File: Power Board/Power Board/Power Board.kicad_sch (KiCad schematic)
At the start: 6 parts, among them J1 MINIFIT-2-VERT, J2 NMJ6HFD2, J3 NMJ6HFD2, J4 MEGAFIT-2-VERT, J5 MINIFIT-2-VERT

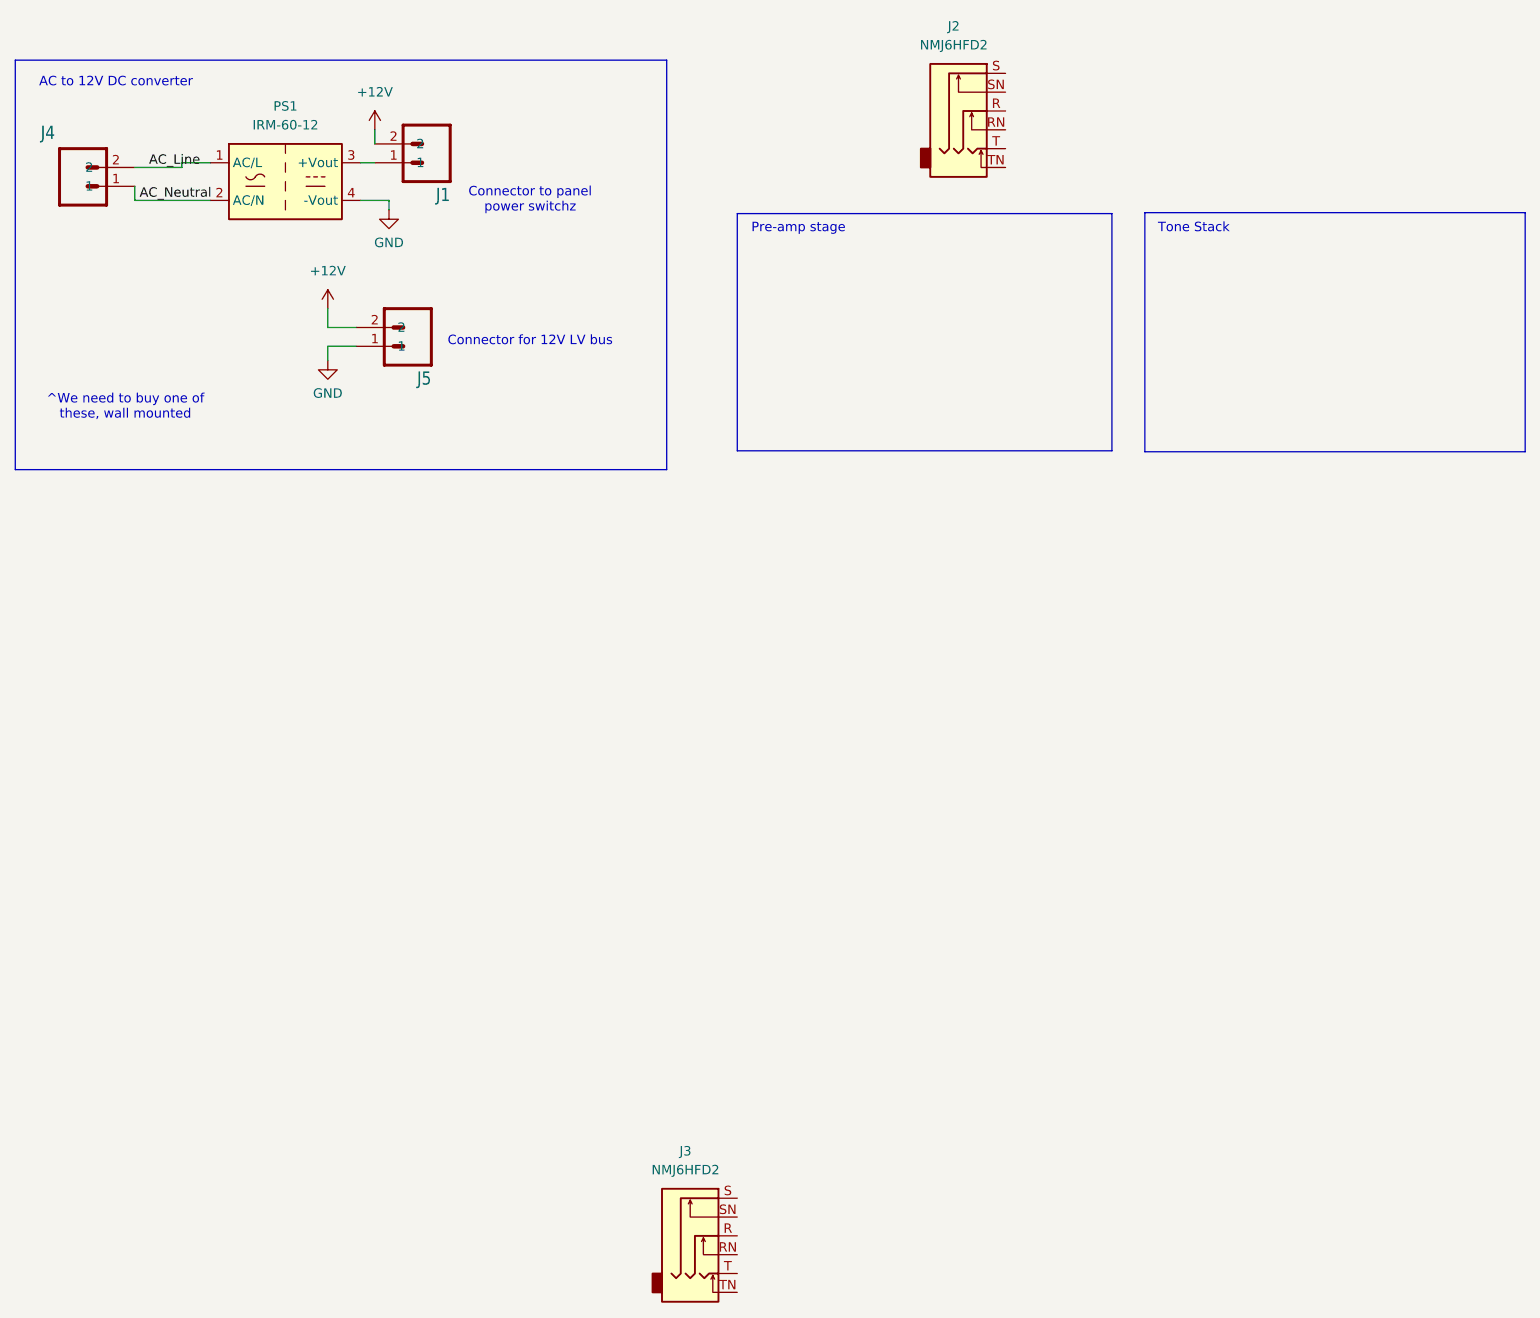
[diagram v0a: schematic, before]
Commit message: Finished schematic and layout of power board
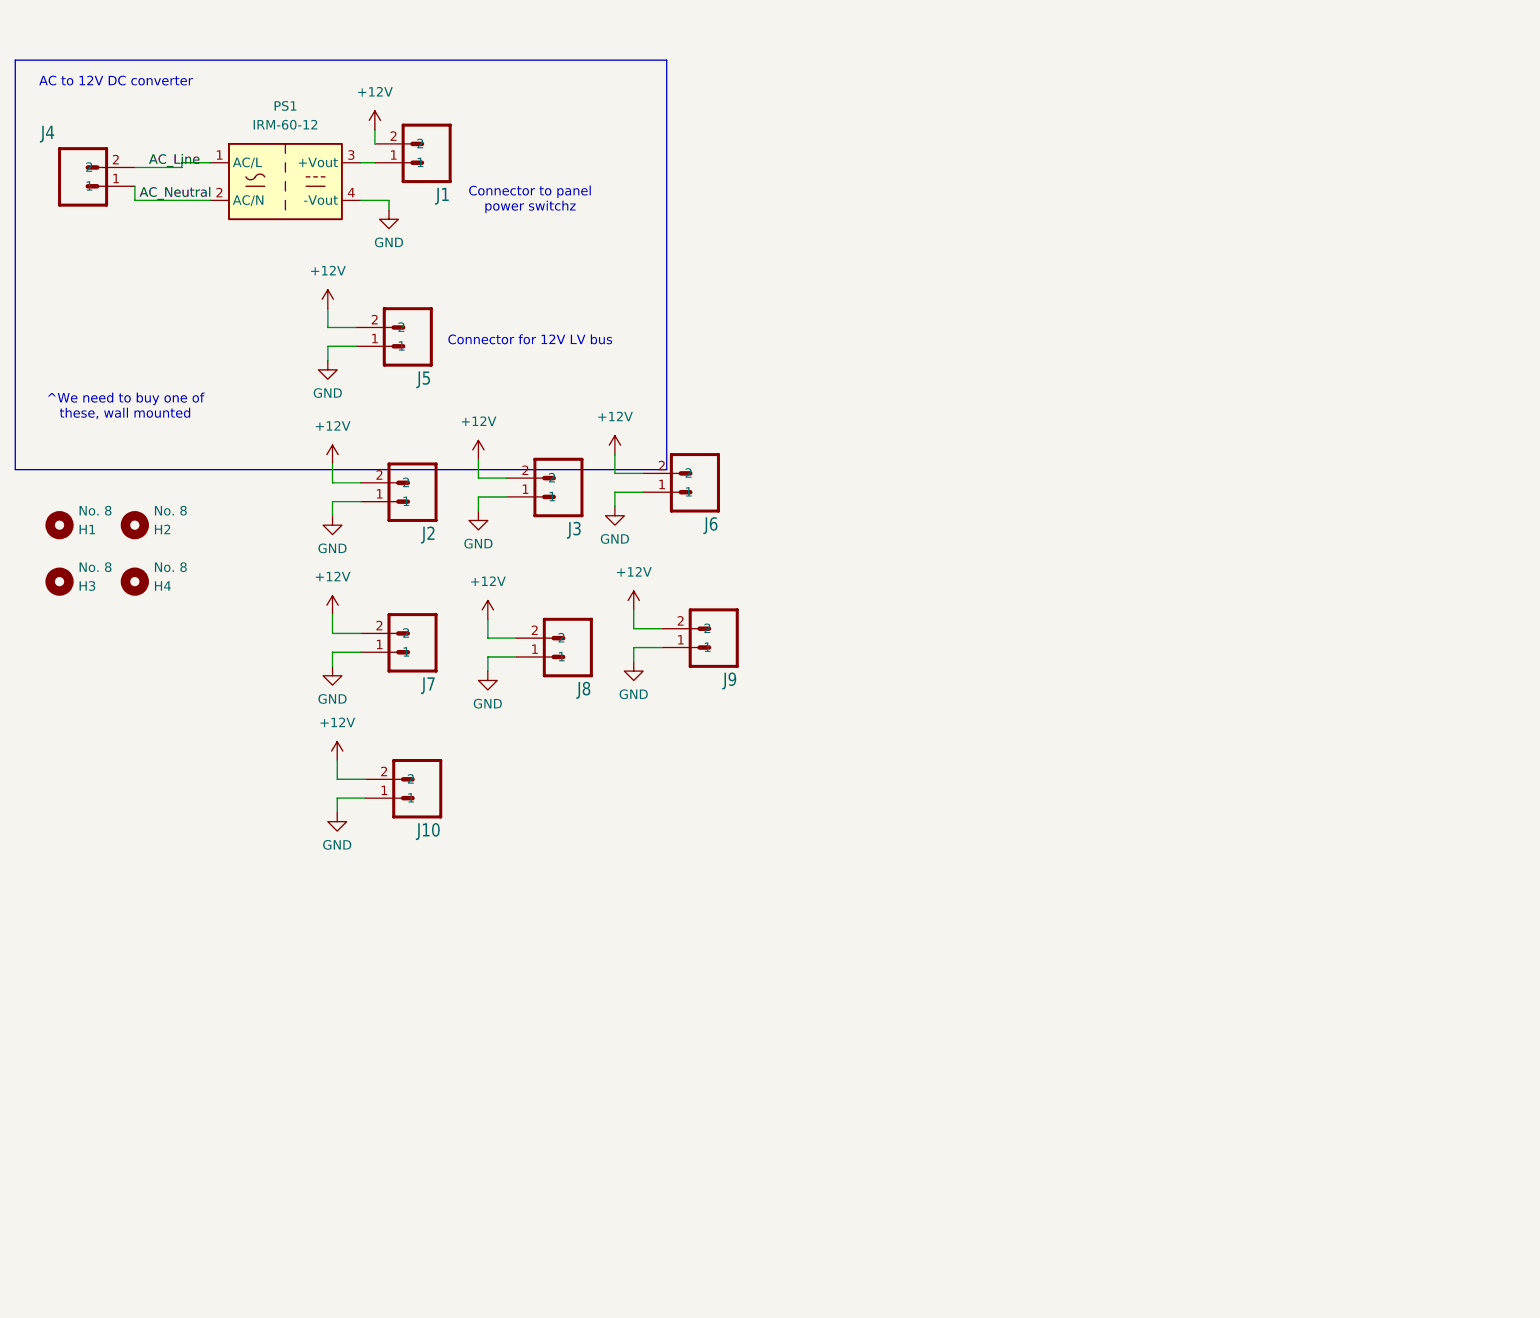
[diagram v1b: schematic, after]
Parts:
- removed J2, J3: NMJ6HFD2, Connector_Audio:Jack_6.35mm_Neutrik_NMJ6HFD2_Horizontal, symbol Connector_Audio:NMJ6HFD2
- added H1, H2, H3, H4: No. 8, MountingHole:MountingHole_3.2mm_M3, symbol Mechanical:MountingHole
- added J10, J2, J3, J6, J7, J8, J9: MINIFIT-2-VERT, Connector_Molex:Molex_Mini-Fit_Jr_5566-02A_2x01_P4.20mm_Vertical, symbol BMS-Master-Revision8-eagle-import:MINIFIT-2-VERT
- J1: footprint Connector_Molex:Molex_Mini-Fit_Jr_5566-02A_2x01_P4.20mm_Vertical -> Connector_Molex:Molex_Mega-Fit_76829-0102_2x01_P5.70mm_Vertical
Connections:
- net +12V: now also J10.2, J2.2, J3.2, J6.2, J7.2, J8.2, J9.2
- net GND: now also J10.1, J2.1, J3.1, J6.1, J7.1, J8.1, J9.1
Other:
- note removed: "Pre-amp stage"
- note removed: "Tone Stack"

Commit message: Completed Power Board
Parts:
- removed J10, J6: MINIFIT-2-VERT, Connector_Molex:Molex_Mini-Fit_Jr_5566-02A_2x01_P4.20mm_Vertical, symbol BMS-Master-Revision8-eagle-import:MINIFIT-2-VERT
- added F1: Fuse, Fuse:Fuseholder_Blade_Mini_Keystone_3568, symbol Device:Fuse
- added J6: ~, Connector_Molex:Molex_Mega-Fit_76829-0004_2x02_P5.70mm_Vertical, symbol Connector_Generic:Conn_02x02_Counter_Clockwise
- added U1: AC025-D24, GTSR_KiCAD_Footprints:AC025-D15, symbol GTSR_symbol_lib:AC025-D15
- J5: footprint Connector_Molex:Molex_Mini-Fit_Jr_5566-02A_2x01_P4.20mm_Vertical -> Connector_Molex:Molex_Micro-Fit_3.0_43650-0215_1x02_P3.00mm_Vertical
- J8: footprint Connector_Molex:Molex_Mini-Fit_Jr_5566-02A_2x01_P4.20mm_Vertical -> Connector_PinHeader_2.54mm:PinHeader_1x02_P2.54mm_Vertical
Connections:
- net +12V: now also F1.2; no longer J1.2, J5.2, J8.2
- net AC_Line: now also U1.3 (AC_Line)
- net AC_Neutral: now also U1.2 (AC_Neutral)
- net GND: now also J6.1 (Pin_1), J6.2 (Pin_2), U1.5 (Com); no longer J5.1, J8.1
- new net: J8.2, U1.1 (Frame_GND)
- new net: F1.1, J1.2
- new net +24V: J6.4 (Pin_4), U1.6 (+Vo)
- new net -24V: J6.3 (Pin_3), U1.4 (-Vo)
- new net Earth_GND: J5.1, J5.2, J8.1
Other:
- moved on the sheet: H1, H2, H3, H4, J2, J3
